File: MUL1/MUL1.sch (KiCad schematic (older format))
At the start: 11 parts, among them J1 Conn_01x08_Male, J2 Conn_01x09_Male, J3 Conn_01x08_Male, J4 Conn_01x01_Male, J5 Conn_01x02_Male, U1 74LS08, U2 74LS283, U3 74LS08, U4 74LS283

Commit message: Polishing MUL. Add gerber.
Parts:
- C1, C2: footprint Capacitor_SMD:C_0805_2012Metric_Pad1.18x1.45mm_HandSolder -> Capacitor_THT:C_Disc_D7.5mm_W5.0mm_P10.00mm
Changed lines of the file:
@@
 F 0 "C2" H 7365 4846 50  0000 L CNN
 F 1 "0.1uF" H 7365 4755 50  0000 L CNN
-F 2 "Capacitor_SMD:C_0805_2012Metric_Pad1.18x1.45mm_HandSolder" H 7288 4650 50  0001 C CNN
+F 2 "Capacitor_THT:C_Disc_D7.5mm_W5.0mm_P10.00mm" H 7288 4650 50  0001 C CNN
 F 3 "~" H 7250 4800 50  0001 C CNN
 	1    7250 4800
@@
 F 0 "C1" H 6865 4846 50  0000 L CNN
 F 1 "0.1uF" H 6865 4755 50  0000 L CNN
-F 2 "Capacitor_SMD:C_0805_2012Metric_Pad1.18x1.45mm_HandSolder" H 6788 4650 50  0001 C CNN
+F 2 "Capacitor_THT:C_Disc_D7.5mm_W5.0mm_P10.00mm" H 6788 4650 50  0001 C CNN
 F 3 "~" H 6750 4800 50  0001 C CNN
 	1    6750 4800

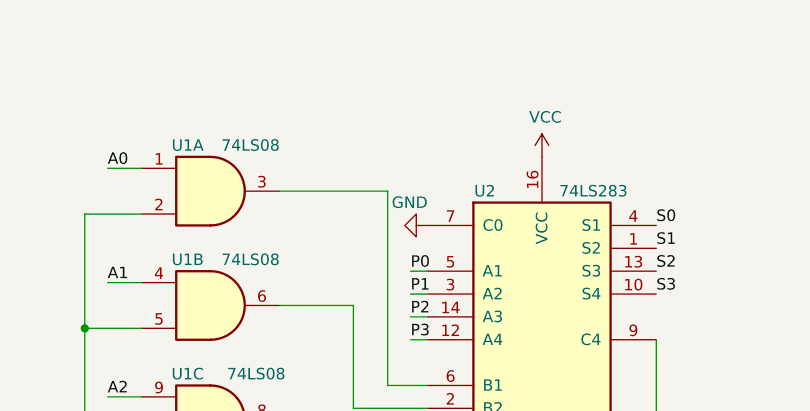
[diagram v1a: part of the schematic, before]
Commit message: Add jumper to MUL1
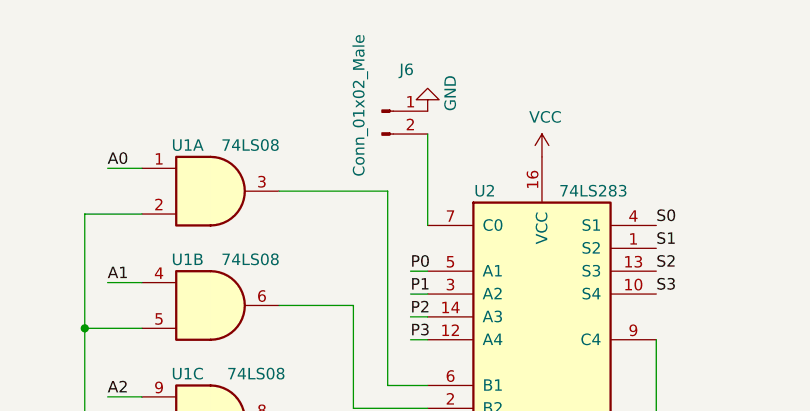
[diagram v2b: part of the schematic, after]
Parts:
- added J6: Conn_01x02_Male, Connector_PinHeader_2.54mm:PinHeader_1x02_P2.54mm_Vertical, symbol Connector:Conn_01x02_Male
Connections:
- net GND: now also J6.1 (Pin_1); no longer U2.7 (C0)
- new net: J6.2 (Pin_2), U2.7 (C0)
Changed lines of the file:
@@
 L power:GND #PWR02
 U 1 1 63764C92
-P 4250 2500
-F 0 "#PWR02" H 4250 2250 50  0001 C CNN
-F 1 "GND" V 4150 2500 50  0000 R CNN
-F 2 "" H 4250 2500 50  0001 C CNN
-F 3 "" H 4250 2500 50  0001 C CNN
-	1    4250 2500
-	0    1    1    0
+P 4250 2000
+F 0 "#PWR02" H 4250 1750 50  0001 C CNN
+F 1 "GND" V 4150 2000 50  0000 R CNN
+F 2 "" H 4250 2000 50  0001 C CNN
+F 3 "" H 4250 2000 50  0001 C CNN
+	1    4250 2000
+	-1   0    0    1
 $EndComp
 $Comp
@@
 	1    0    0    -1
 $EndComp
+$Comp
+L Connector:Conn_01x02_Male J6
+U 1 1 63E55B5B
+P 4050 2000
+F 0 "J6" H 4158 2181 50  0000 C CNN
+F 1 "Conn_01x02_Male" V 3950 2025 50  0000 C CNN
+F 2 "Connector_PinHeader_2.54mm:PinHeader_1x02_P2.54mm_Vertical" H 4050 2000 50  0001 C CNN
+F 3 "~" H 4050 2000 50  0001 C CNN
+	1    4050 2000
+	1    0    0    -1
+$EndComp
+Wire Wire Line
+	4250 2100 4250 2500
 $EndSCHEMATC

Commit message: Polishing MUL1
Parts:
- removed J6: Conn_01x02_Male, Connector_PinHeader_2.54mm:PinHeader_1x02_P2.54mm_Vertical, symbol Connector:Conn_01x02_Male
- added J6: Conn_01x01_Male, Connector_PinHeader_2.54mm:PinHeader_1x01_P2.54mm_Vertical, symbol Connector:Conn_01x01_Male
- added R1: 10k, Resistor_SMD:R_0805_2012Metric_Pad1.20x1.40mm_HandSolder, symbol Device:R
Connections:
- net GND: now also R1.1
- net at U2.7 (C0): now also J6.1 (Pin_1), R1.2
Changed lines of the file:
@@
 L power:GND #PWR02
 U 1 1 63764C92
-P 4250 2000
-F 0 "#PWR02" H 4250 1750 50  0001 C CNN
-F 1 "GND" V 4150 2000 50  0000 R CNN
-F 2 "" H 4250 2000 50  0001 C CNN
-F 3 "" H 4250 2000 50  0001 C CNN
-	1    4250 2000
+P 4250 1800
+F 0 "#PWR02" H 4250 1550 50  0001 C CNN
+F 1 "GND" V 4150 1800 50  0000 R CNN
+F 2 "" H 4250 1800 50  0001 C CNN
+F 3 "" H 4250 1800 50  0001 C CNN
+	1    4250 1800
 	-1   0    0    1
 $EndComp
@@
 	1    0    0    -1
 $EndComp
-$Comp
-L Connector:Conn_01x02_Male J6
-U 1 1 63E55B5B
-P 4050 2000
-F 0 "J6" H 4158 2181 50  0000 C CNN
-F 1 "Conn_01x02_Male" V 3950 2025 50  0000 C CNN
-F 2 "Connector_PinHeader_2.54mm:PinHeader_1x02_P2.54mm_Vertical" H 4050 2000 50  0001 C CNN
-F 3 "~" H 4050 2000 50  0001 C CNN
-	1    4050 2000
-	1    0    0    -1
-$EndComp
 Wire Wire Line
 	4250 2100 4250 2500
+$Comp
+L Connector:Conn_01x01_Male J6
+U 1 1 63ED31D3
+P 4050 2100
+F 0 "J6" H 4075 2175 50  0000 C CNN
+F 1 "Conn_01x01_Male" H 4050 2000 50  0000 C CNN
+F 2 "Connector_PinHeader_2.54mm:PinHeader_1x01_P2.54mm_Vertical" H 4050 2100 50  0001 C CNN
+F 3 "~" H 4050 2100 50  0001 C CNN
+	1    4050 2100
+	1    0    0    -1
+$EndComp
+$Comp
+L Device:R R1
+U 1 1 63ED60D5
+P 4250 1950
+F 0 "R1" H 4300 1925 50  0000 L CNN
+F 1 "10k" V 4250 1875 50  0000 L CNN
+F 2 "Resistor_SMD:R_0805_2012Metric_Pad1.20x1.40mm_HandSolder" V 4180 1950 50  0001 C CNN
+F 3 "~" H 4250 1950 50  0001 C CNN
+	1    4250 1950
+	1    0    0    -1
+$EndComp
+Connection ~ 4250 2100
 $EndSCHEMATC
